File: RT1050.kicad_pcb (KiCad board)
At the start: 4 copper layers, 88 x 94.5 mm, 109 parts, among them IC1 IS42S16160J-6BLI, IC2 S26KL512SDABHV020, J1 Conn_01x04_Pin, J10 Conn_01x06_Pin, J13 Conn_02x04_Counter_Clockwise, J14 Conn_02x04_Counter_Clockwise, J2 Conn_01x04_Pin, J3 Conn_01x20, J4 Conn_01x05_Pin, J5 USB_C_Receptacle_USB2.0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

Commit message: SDRAM redo and finished boards
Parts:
- moved IC1 6.28 mm to (138.8, 86.4)
- moved C34 0.13 mm to (163.8, 113.4)
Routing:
- net DQ15: track 24.5 -> 0.00 mm
- net DQ14: track 24.2 -> 0.00 mm
- net DQ1: track 22.9 -> 0.00 mm
- net DQ11: track 22.8 -> 0.00 mm, vias 2 -> 1
- net DQ13: track 22.8 -> 0.51 mm, vias 2 -> 1
- net DQ6: track 22.0 -> 0.00 mm, vias 1 -> 0
- net DQ0: track 21.5 -> 0.00 mm, vias 2 -> 1
- net DQMH: track 22.1 -> 0.57 mm
- net DQ8: track 21.5 -> 0.00 mm, vias 2 -> 1
- net DQ12: track 21.4 -> 0.00 mm, vias 2 -> 1
- net DQ2: track 21.3 -> 0.00 mm, vias 2 -> 1
- net DQ5: track 21.0 -> 0.00 mm
- net DQ10: track 21.4 -> 0.46 mm, vias 2 -> 1
- net DQ9: track 20.8 -> 0.00 mm, vias 2 -> 1
- net DQ3: track 19.8 -> 0.00 mm, vias 2 -> 1
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
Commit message: SDRAM redo and finished boards
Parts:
- IC1: moved to F.Cu
- J4: footprint Connector_PinHeader_2.00mm:PinHeader_1x05_P2.00mm_Vertical -> Connector_PinHeader_2.00mm:PinHeader_1x04_P2.00mm_Vertical
- moved IC1 3.00 mm to (141.8, 86.2)
- moved C58 0.58 mm to (163.3, 83.8), turned to 90 degrees
- moved C37 0.41 mm to (162.6, 83.8), turned to 90 degrees
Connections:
- U1 pad D9: SHDN -> unconnected-(U1A-GPIO_B0_10-PadD9)
- U9 pad 14: unconnected-(U9-GP5-Pad14) -> SHDN
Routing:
- net STB: track 0.05 -> 39.6 mm, vias 1 -> 4
- net A5: track 0.00 -> 32.2 mm, vias 1 -> 2
- net A4: track 0.00 -> 31.4 mm
- net A2: track 0.00 -> 31.2 mm, vias 1 -> 0
- net A3: track 0.21 -> 31.4 mm
- net A1: track 0.00 -> 31.1 mm, vias 1 -> 0
- net ~{WE}: track 0.00 -> 30.5 mm
- net DQ8: track 0.00 -> 30.1 mm, vias 1 -> 2
- net DQML: track 0.14 -> 30.1 mm, vias 1 -> 2
- net DQMH: track 0.57 -> 30.3 mm, vias 1 -> 2
- net DQ0: track 0.00 -> 29.7 mm, vias 1 -> 2
- net A8: track 0.00 -> 29.1 mm, vias 1 -> 0
- net A11: track 0.00 -> 28.8 mm
- net A7: track 0.00 -> 28.8 mm, vias 1 -> 0
- net A12: track 0.00 -> 28.8 mm, vias 1 -> 0
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- added copper zone on F.Cu, net GND

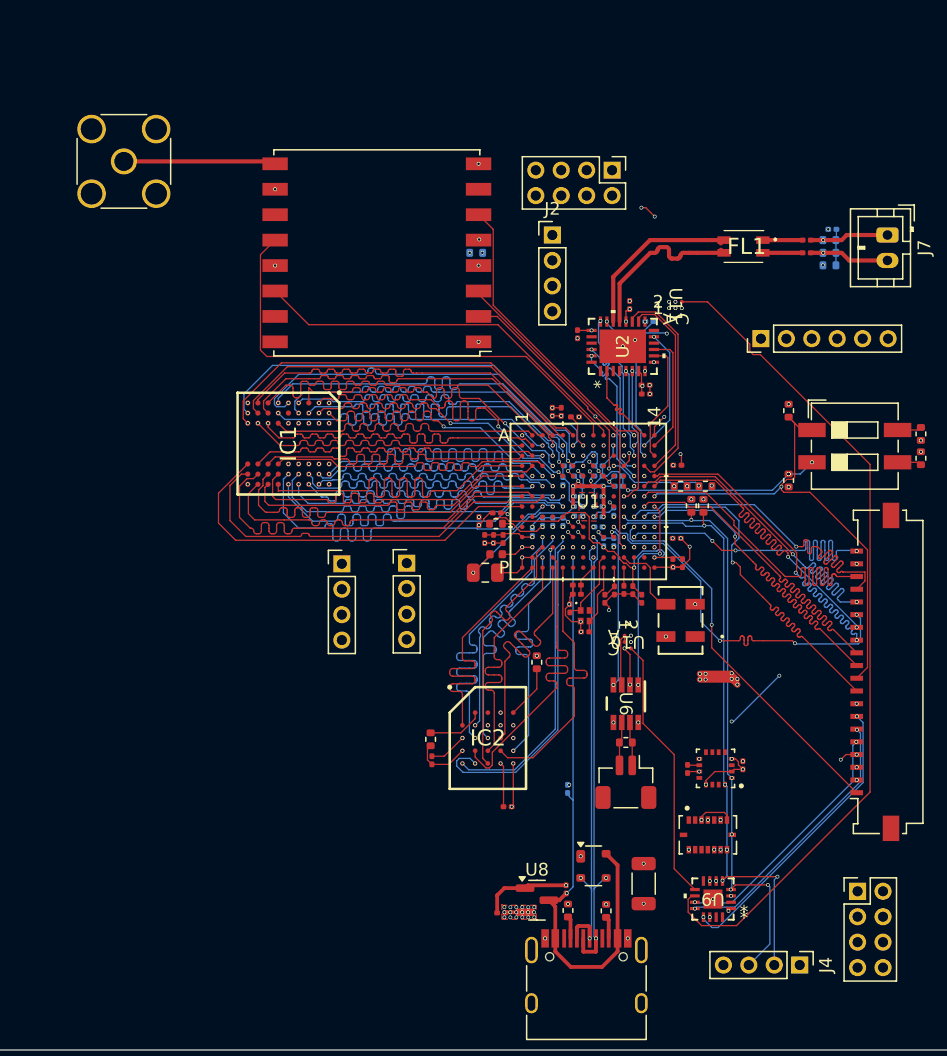
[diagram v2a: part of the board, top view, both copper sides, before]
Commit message: added FRAM
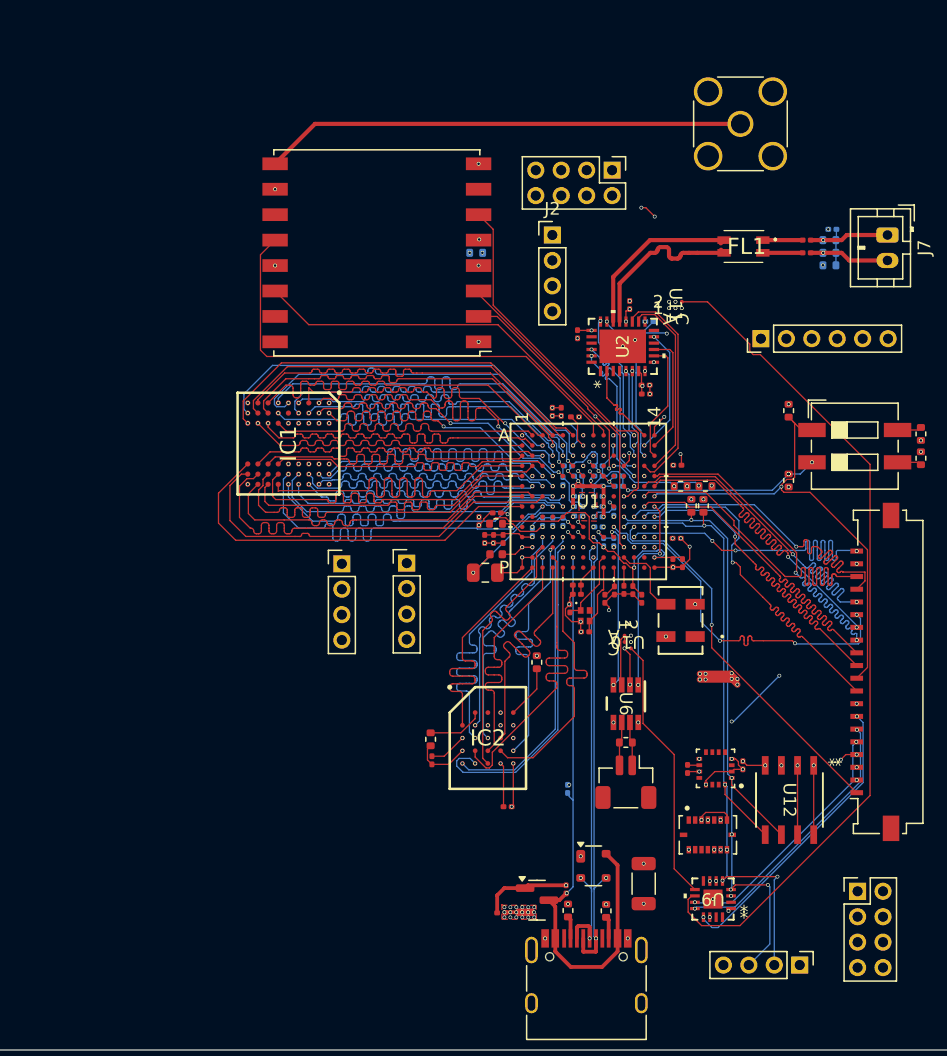
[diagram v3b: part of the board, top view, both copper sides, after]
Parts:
- added U12: CY15B064J-SXET, footprints:SO8_CY15_CYP, F.Cu at (181.2, 114.3)
- moved J8 48.6 mm to (177.4, 61.1)
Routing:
- net Net-(J8-In): track 12.0 -> 38.2 mm
- net GND: track 71.1 -> 78.5 mm, vias 85 -> 88
- net LPI2C1_SCL: track 47.4 -> 53.5 mm
- net +3.3V: track 49.7 -> 55.1 mm, vias 72 -> 73
- net LPI2C1_SDA: track 48.3 -> 53.5 mm

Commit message: updated schem pdf
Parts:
- moved J7 89.0 mm to (101.5, 53.3)
- moved C10 89.0 mm to (85.0, 71.5)
- moved C11 89.0 mm to (77.1, 80.9)
- moved C12 89.0 mm to (77.1, 81.6)
- moved C13 89.0 mm to (84.7, 79.2)
- moved C14 89.0 mm to (85.4, 79.2)
- moved C15 89.0 mm to (80.0, 77.5)
- moved C17 89.0 mm to (81.5, 81.3)
- moved C22 89.0 mm to (77.8, 84.6)
- moved C27 89.0 mm to (73.6, 76.7)
- moved C28 89.0 mm to (69.8, 77.3)
- moved C30 89.0 mm to (69.9, 79.9)
- moved C31 89.0 mm to (74.4, 75.9)
- moved C34 89.0 mm to (76.4, 96.9)
- moved C35 89.0 mm to (76.4, 71.5)
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
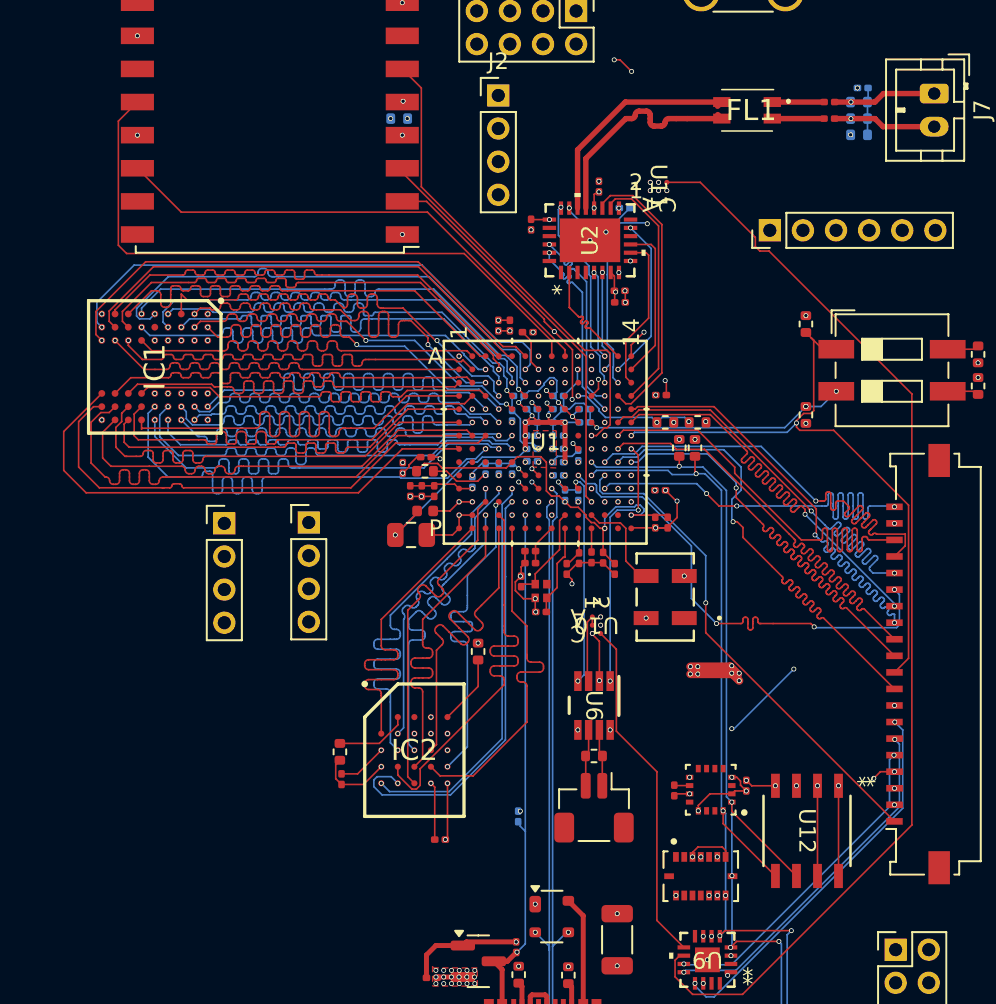
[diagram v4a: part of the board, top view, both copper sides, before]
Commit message: cleaned up and dealt with drc
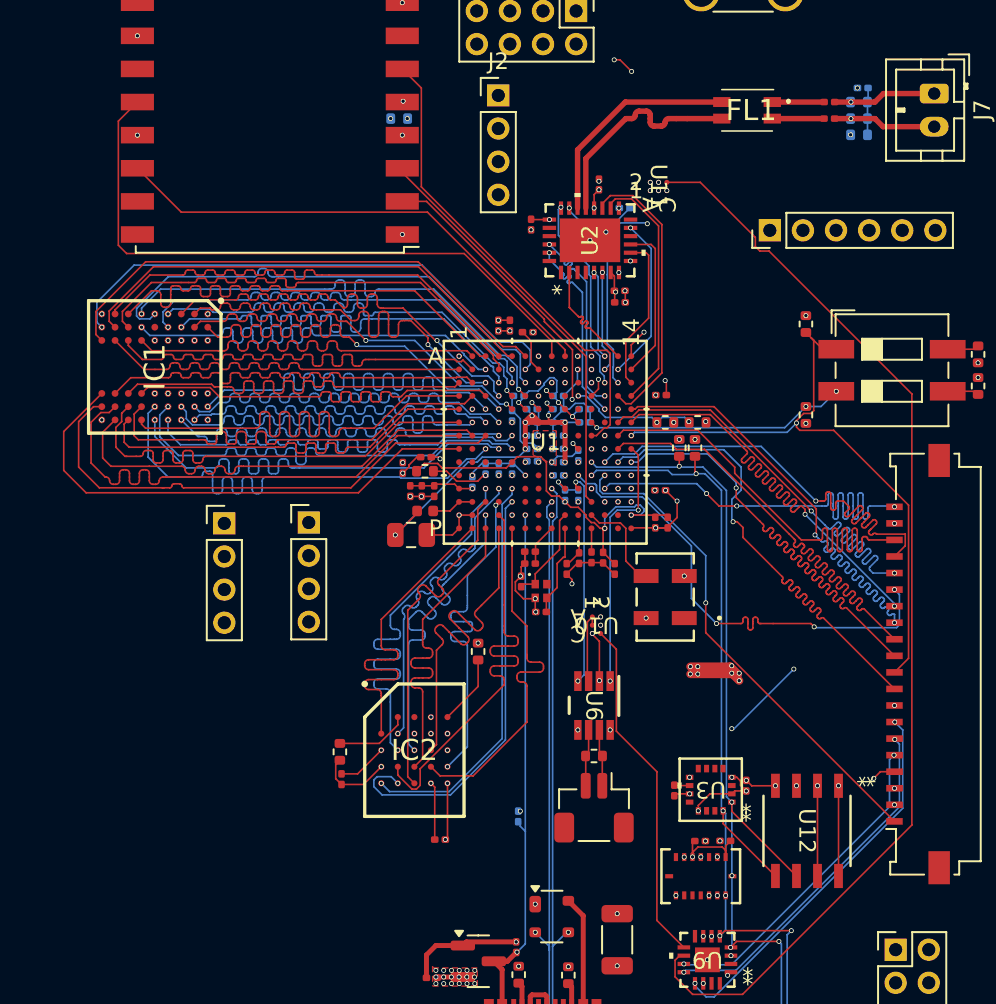
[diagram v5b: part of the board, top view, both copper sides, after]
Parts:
- added C52: 100nF, Capacitor_SMD:C_0201_0603Metric, F.Cu at (87.4, 98.4)
- added C62: 100nF, Capacitor_SMD:C_0201_0603Metric, F.Cu at (88.9, 98.4)
- U3: footprint footprints:PQFN50P300X300X100-16N -> footprints:MMC5983MA_MEM
- U4: footprint footprints:PQFN50P450X300X100-16N -> footprints:QFN_BMI085_BOS
- moved C46 0.13 mm to (81.2, 58.8)
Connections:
- U4 pad 2: unconnected-(U4-NC-Pad2) -> GND
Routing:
- net +3.3V: track 55.1 -> 57.2 mm
- net DQ12: track 27.6 -> 26.7 mm
- net WAKEUP: track 0.57 -> 0.00 mm, vias 1 -> 0
- net PMIC_STBY_REQ: track 0.57 -> 0.00 mm, vias 1 -> 0
- net PMIC_ON_REQ: track 0.57 -> 0.00 mm, vias 1 -> 0
- net GND: track 78.5 -> 78.6 mm, vias 88 -> 91
- net RESET: vias 1 -> 0
- net ONOFF: vias 1 -> 0
- net Net-(L1-Pad2): vias 2 -> 0
- net LPSPI3_SDO: vias 3 -> 2
- net LPSPI3_SDI: vias 1 -> 0
- net LPI2C2_SCL: vias 3 -> 2
- net HOPERF_RST: vias 1 -> 0
- net GPIO_AD_B0_04: vias 4 -> 3
- net ENET_TX_ER: vias 1 -> 0
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
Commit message: quick fix
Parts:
- C28: footprint Capacitor_SMD:C_0201_0603Metric -> Capacitor_SMD:C_0603_1608Metric
- C32, C51: footprint Capacitor_SMD:C_0201_0603Metric -> Capacitor_SMD:C_0402_1005Metric
- moved C28 2.83 mm to (67.4, 78.7)
- moved C51 0.30 mm to (85.5, 95.3)
- moved C32 0.23 mm to (85.2, 77.2)
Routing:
- net +3.3V: track 57.2 -> 62.8 mm, vias 73 -> 74
- net GND: track 78.6 -> 81.9 mm

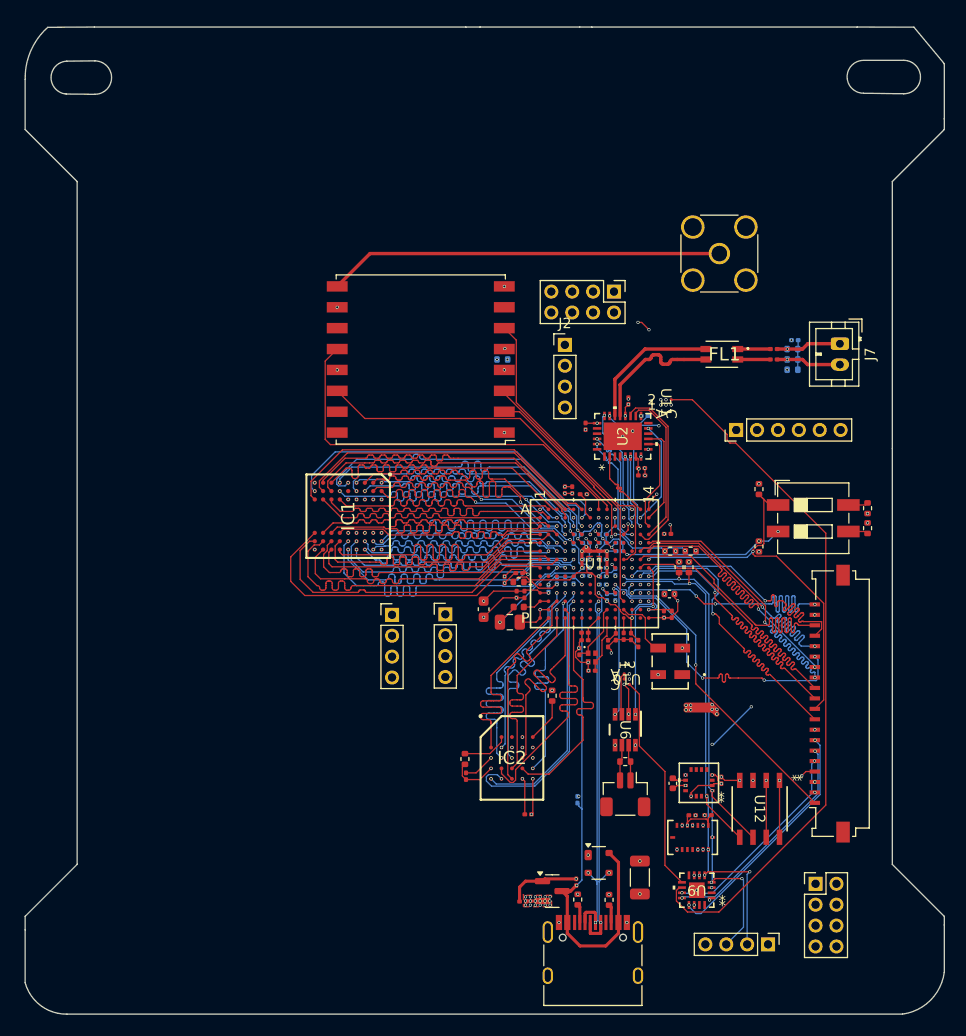
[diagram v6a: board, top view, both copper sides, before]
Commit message: changes to board due to availability of components
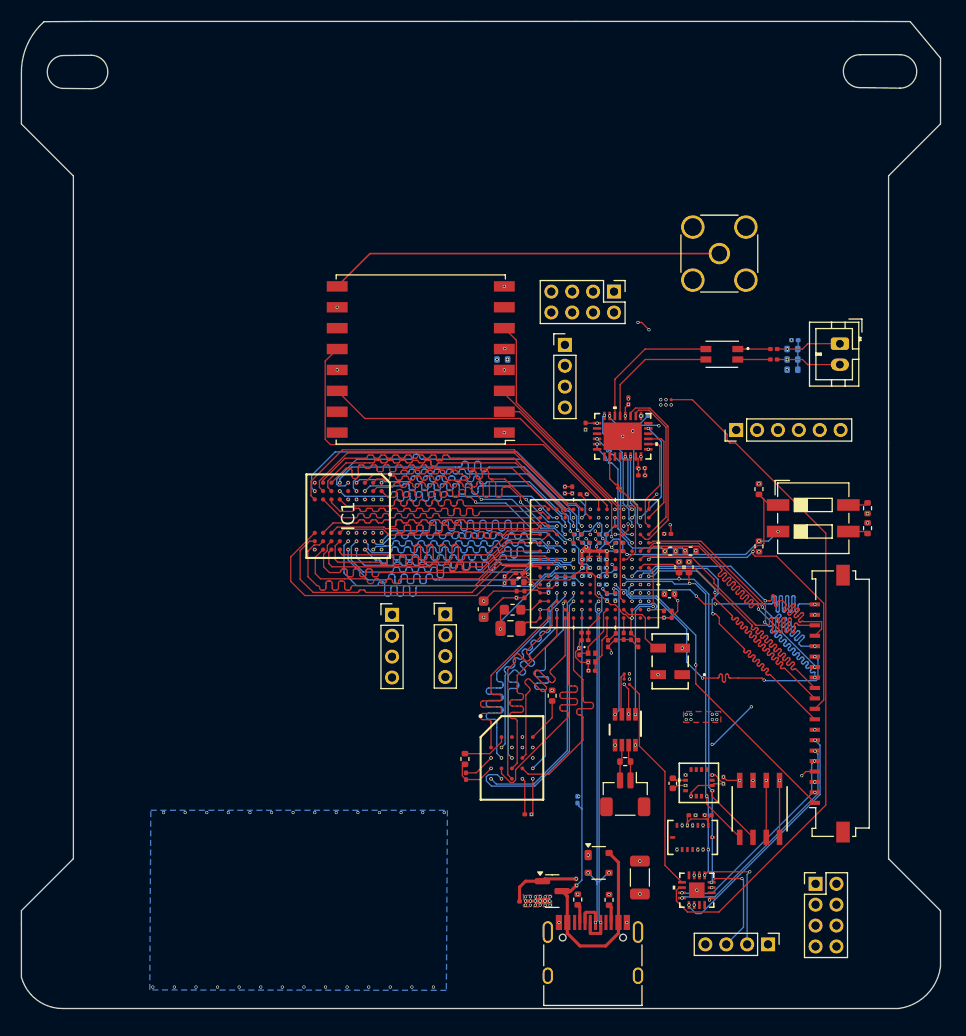
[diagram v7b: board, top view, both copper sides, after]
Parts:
- added G***: LOGO, LOGO, B.Cu at (42.0, 108.8)
- C55, C56: value 100n -> 100nF
- L1: footprint Inductor_SMD:L_0402_1005Metric -> Inductor_SMD:L_0603_1608Metric
- moved L1 0.64 mm to (70.2, 78.7)
- moved C30 0.60 mm to (70.0, 80.5)
- moved C50 0.20 mm to (90.3, 95.1)
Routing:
- net +3.3V: track 62.8 -> 56.9 mm
- net TRD_P: track 13.4 -> 12.2 mm
- net DCDC_OUT: track 28.5 -> 29.1 mm
- net GND: vias 91 -> 119
- added copper zone on B.Cu, net GND
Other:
- board text added: "Designed by Madhav Kapa"
- board text added: "Project Horizon"
